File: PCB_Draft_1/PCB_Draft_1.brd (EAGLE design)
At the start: 63.5 x 35.6 mm, 13 parts, among them IC1 L6205PD

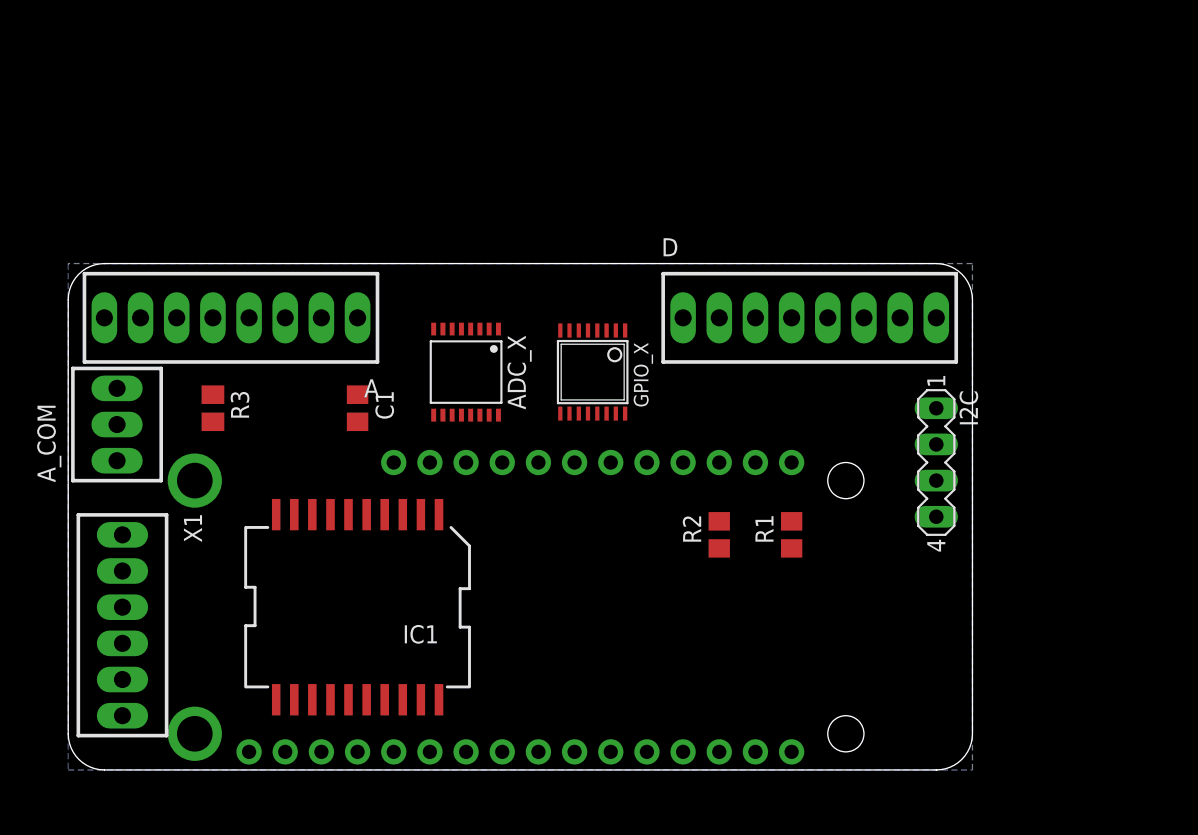
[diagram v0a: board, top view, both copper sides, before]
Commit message: Restarted schematic on larger sheet format. Added second motor driver
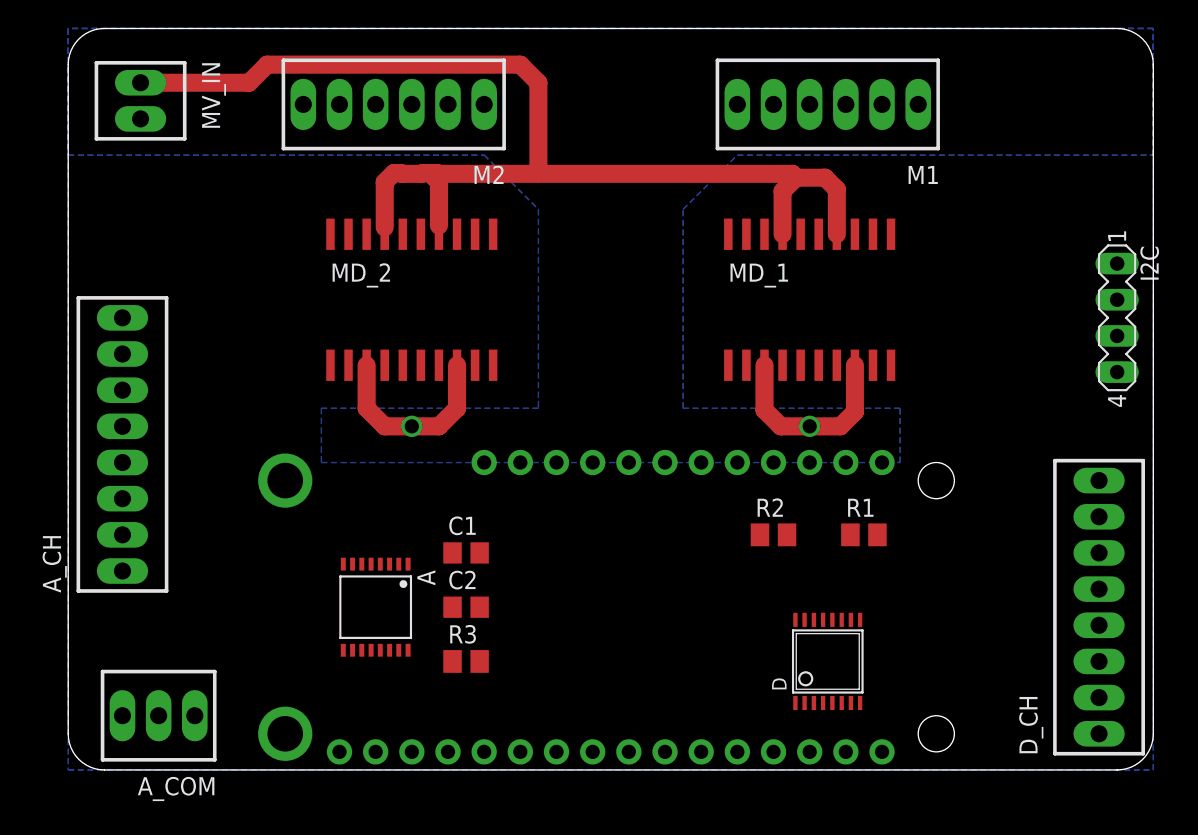
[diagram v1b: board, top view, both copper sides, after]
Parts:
- removed ADC_X: ADS7828, burr-brown:TSSOP16-PW
- removed GPIO_X: PCA9534PW, micro-philips:TSSOP16
- removed IC1: L6205PD, st-microelectronics:POWERSO-20
- removed MS1: FEATHERWINGEXTENDED_BOTH_ENDS, ME507:FEATHERWING
- removed X1: (no value), ME507:6POL254
- added A_CH, D_CH: (no value), ME507:8POL254
- added C2: (no value), rcl:C0805
- added FTHRWNG: FEATHERWINGEXTENDED_BOTH_ENDS, ME507:FEATHERWING
- added M1, M2: (no value), ME507:6POL254
- added MD_1, MD_2: L6205D, st-microelectronics:SO20
- added MV_IN: (no value), ME507:2POL254
- A: value (none) -> ADS7828; device ME507:8POL254 -> burr-brown:TSSOP16-PW
- C1: value 5u -> (none)
- D: value (none) -> PCA9534PW; device ME507:8POL254 -> micro-philips:TSSOP16
- R1, R2: device rcl:R0805 -> rcl:M0805
- moved R3 25.1 mm to (27.9, 7.62), turned to 0 degrees
- moved D 24.2 mm to (53.3, 7.62)
- moved A 22.7 mm to (21.6, 11.4)
- moved A_COM 20.7 mm to (6.35, 3.81), turned to 180 degrees
- moved I2C 16.3 mm to (73.7, 31.8)
- moved C1 12.7 mm to (27.9, 15.2), turned to 0 degrees
- moved R1 5.08 mm to (55.9, 16.5), turned to 0 degrees
- moved R2 3.81 mm to (49.5, 16.5), turned to 0 degrees
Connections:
- removed net 3V: ADC_X.16, A_COM.1, GPIO_X.16, I2C.1, MS1.2, R1.1, R2.1
- removed net A_COM: ADC_X.11, A_COM.3, C1.2, R3.1
- removed net INT: GPIO_X.13, MS1.19
- removed net N$18: IC1.9, X1.3
- removed net N$25: IC1.14, MS1.21
- removed net V_MOT: IC1.19, IC1.2, X1.1
- new net 3.3V: A.16, A_COM.1, C1.1, D.16, FTHRWNG.2, I2C.1, R1.1, R2.1
- new net 9V: MD_1.14, MD_1.17, MD_2.14, MD_2.17, MV_IN.1
- new net COM: A.11, A_COM.3, R3.1
- new net MGND: MD_1.3, MD_1.8, MD_2.3, MD_2.8, MV_IN.2
- new net N$23: M1.5, MD_1.13
- new net N$27: M2.4, MD_2.18
- new net N$28: M2.5, MD_2.13
- new net N$29: FTHRWNG.20, MD_2.10
- new net N$30: FTHRWNG.22, MD_2.9
- new net N$31: FTHRWNG.21, MD_2.2
- new net N$32: FTHRWNG.23, MD_2.1
- new net N$33: FTHRWNG.10, MD_1.1
- new net N$34: FTHRWNG.8, MD_1.2
- new net N$35: FTHRWNG.9, MD_1.9
- new net N$36: FTHRWNG.7, MD_1.10
- new net N$37: FTHRWNG.24, MD_2.11
- new net N$38: FTHRWNG.25, MD_2.20
- new net N$39: FTHRWNG.6, MD_1.20
- new net N$40: FTHRWNG.5, MD_1.11
- net GND: now also A.12, A.13, A.9, C1.2, C2.2, D.1, D.2, D.3, D.8, FTHRWNG.4, MD_1.15, MD_1.16, MD_1.5, MD_1.6, MD_2.15, MD_2.16, MD_2.5, MD_2.6; no longer ADC_X.12, ADC_X.13, ADC_X.9, GPIO_X.1, GPIO_X.2, GPIO_X.3, GPIO_X.8, IC1.1, IC1.10, IC1.11, IC1.13, IC1.20, IC1.8, MS1.4, X1.2
- net N$1: now also D.12, D_CH.1; no longer D.1, GPIO_X.4
- net N$10: now also A_CH.7; no longer ADC_X.2
- net N$11: now also A_CH.6; no longer ADC_X.3
- net N$12: now also A_CH.5; no longer ADC_X.4
- net N$13: now also A_CH.4; no longer ADC_X.5
- net N$14: now also A_CH.3; no longer ADC_X.6
- net N$15: now also A_CH.2; no longer ADC_X.7
- net N$16: now also A_CH.1; no longer ADC_X.8
- net N$17: now also A.10, C2.1; no longer ADC_X.10, C1.1
- net N$19: now also D.13, FTHRWNG.19; no longer IC1.3, X1.4
- net N$2: now also D.11, D_CH.2; no longer D.2, GPIO_X.5
- net N$20: now also M1.1, MD_1.4; no longer IC1.12, X1.5
- net N$21: now also M1.2, MD_1.7; no longer IC1.18, X1.6
- net N$22: now also M1.4, MD_1.18; no longer IC1.6, MS1.23
- net N$24: now also M2.1, MD_2.4; no longer IC1.15, MS1.20
- net N$26: now also M2.2, MD_2.7; no longer IC1.7, MS1.22
- net N$3: now also D.10, D_CH.3; no longer D.3, GPIO_X.6
- net N$4: now also D.9, D_CH.4; no longer D.4, GPIO_X.7
- net N$5: now also D.7, D_CH.5; no longer D.5, GPIO_X.9
- net N$6: now also D_CH.6; no longer GPIO_X.10
- net N$7: now also D.5, D_CH.7; no longer D.7, GPIO_X.11
- net N$8: now also D.4, D_CH.8; no longer D.8, GPIO_X.12
- net N$9: now also A_CH.8; no longer ADC_X.1
- net SCL: now also A.14, D.14, FTHRWNG.18; no longer ADC_X.14, GPIO_X.14, MS1.18
- net SDA: now also A.15, D.15, FTHRWNG.17; no longer ADC_X.15, GPIO_X.15, MS1.17
- net VBOOT: now also MD_1.12, MD_2.12; no longer IC1.17
- net VCP: now also MD_1.19, MD_2.19; no longer IC1.4
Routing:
- net 9V: track 0.00 -> 82.5 mm
- net MGND: track 0.00 -> 27.1 mm, vias 0 -> 2
- added copper zone on layer 16, net MGND
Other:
- board size 63.5 x 35.6 mm -> 76.2 x 52.1 mm
